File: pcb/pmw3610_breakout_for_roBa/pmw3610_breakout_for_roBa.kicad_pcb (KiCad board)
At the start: 2 copper layers, 22 x 23.5 mm, 13 parts, among them J1 Conn_01x08, U1 MCP1700T-1802E/TT, U2 PMW3610

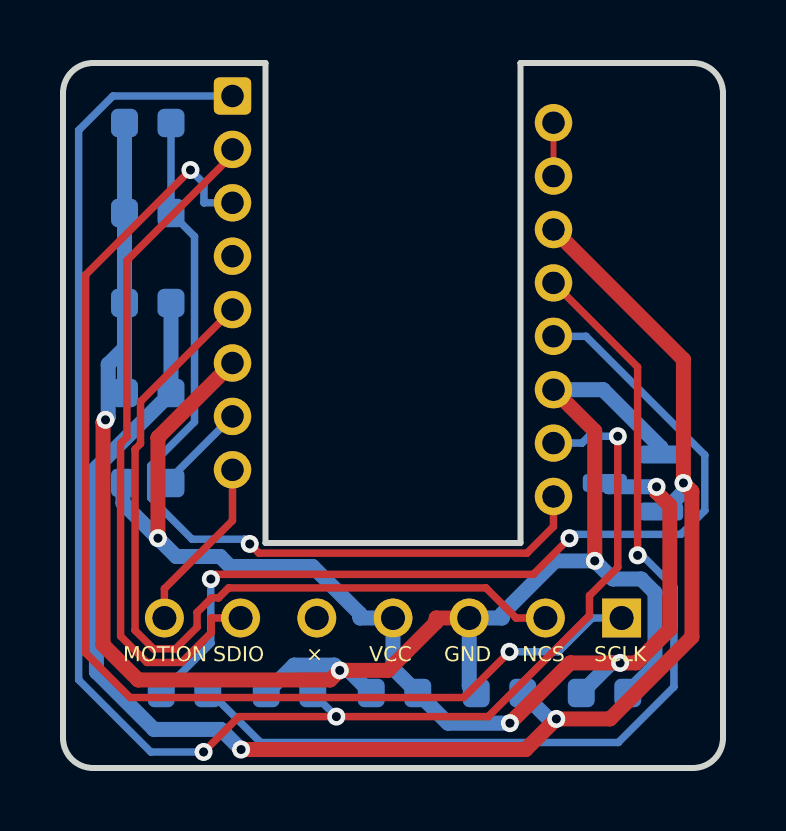
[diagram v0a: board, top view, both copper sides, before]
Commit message: Add VIK connector to trackball PCB, Remove earlier revisions
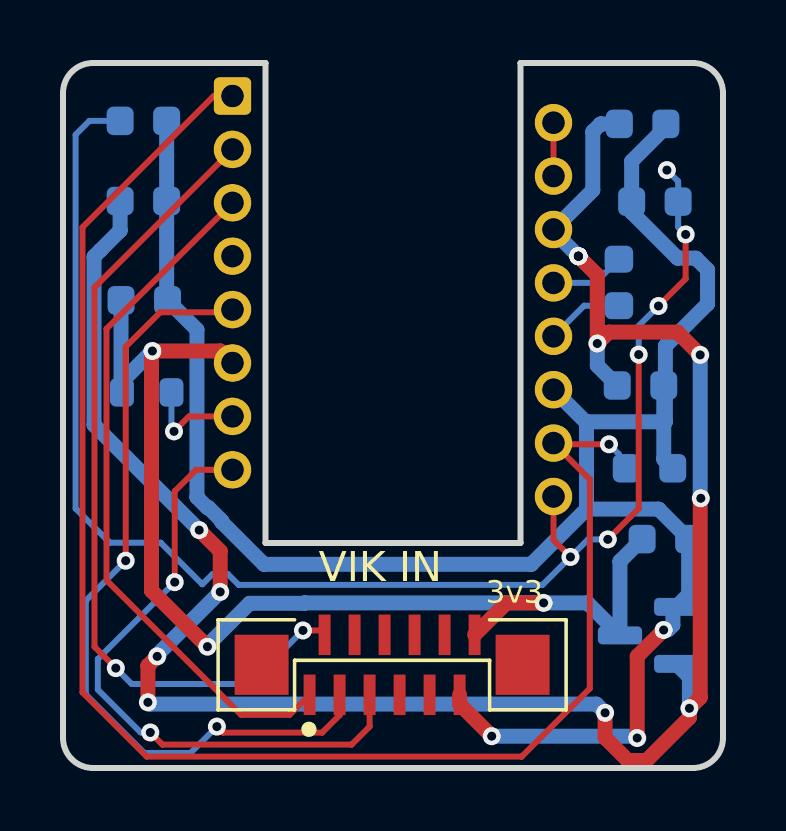
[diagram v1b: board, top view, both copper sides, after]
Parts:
- removed J1: Conn_01x08, roBa:pmw3610_connector_b
- added J2: vik-module-connector, vik:vik-module-connector-vertical, F.Cu at (136.0, 100.1)
- C5: value 100n (X7R) -> 100n (X7R)
- C6: value 10u (X7R) -> 10u (X7R)
- C7: value 10n (X7R) -> 10n (X7R)
- moved C2 20.2 mm to (127.7, 84.6), turned to 0 degrees
- moved C5 19.9 mm to (143.5, 87.3), turned to -90 degrees
- moved C8 17.5 mm to (144.3, 82.0), turned to 0 degrees
- moved C6 17.1 mm to (144.7, 84.6)
- moved C9 16.4 mm to (144.2, 90.8), turned to 0 degrees
- moved C3 15.5 mm to (127.7, 87.9), turned to 0 degrees
- moved C4 14.1 mm to (144.6, 93.5), turned to 0 degrees
- moved C1 5.52 mm to (145.1, 95.9)
- moved U1 5.10 mm to (144.5, 99.1)
- moved C7 3.07 mm to (127.7, 81.9), turned to 0 degrees
- moved R1 3.02 mm to (127.8, 91.0)
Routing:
- net Net-(U2-CN): track 32.2 -> 2.64 mm, vias 1 -> 0
- net Net-(U2-CP): track 30.4 -> 2.60 mm, vias 2 -> 0
- net Net-(U2-VCP): track 29.0 -> 49.8 mm, vias 1 -> 6
- net SCLK: track 39.4 -> 23.2 mm, vias 2 -> 0
- net MOTION: track 5.88 -> 21.1 mm, vias 0 -> 2
- net +1V9: track 54.1 -> 68.4 mm, vias 3 -> 12
- net GND: track 61.8 -> 68.6 mm
- net SDIO: track 23.0 -> 27.5 mm, vias 0 -> 2
- net Net-(U2-+VCSEL): track 53.5 -> 52.3 mm, vias 3 -> 1
- net NCS: track 27.5 -> 26.9 mm, vias 0 -> 2
- net Net-(U2-NRESET): track 3.05 -> 3.49 mm, vias 0 -> 1
- net VCC: track 39.6 -> 39.4 mm, vias 4 -> 3
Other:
- board text removed: "GND"
- board text removed: "MOTION"
- board text removed: "NCS"
- board text removed: "SCLK"
- board text removed: "SDIO"
- board text removed: "VCC"
- board text removed: "×"
